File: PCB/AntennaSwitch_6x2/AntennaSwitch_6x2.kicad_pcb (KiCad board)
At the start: 2 copper layers, 100 x 100 mm, 160 parts, among them J1 Conn_01x08, J2 Conn_01x08, J3 Conn_01x08, J4 HR913550A, J5 SWD, J6 485, J7 12VDC, J8 Conn_01x01, Q1 2N7002K, SW1 LOAD, SW2 SRBV170501, SW3 SRBV170501, SW4 M/R, SW5 RESET, U1 74HC238, U10 74HC148, U11 74HC148, U12 4511, U13 4511, U14 Blue 0.59'', U15 Blue 0.59'', U16 STM32F030F4Px, U17 MAX485E, U18 CH395Q, U19 AZ1117-1.8, U2 74HC573, U20 SY8303, U3 74HC573, U4 74HC238, U5 74HC00, U6 74HC00, U7 74HC00, U8 74HC04, U9 TLC555, Y1 30MHz

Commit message: Relay Board SCH
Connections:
- net GND renamed chasis
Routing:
- net Net-(R68-Pad2): track 30.4 -> 20.7 mm
- net +3V3: track 887.9 -> 886.3 mm
- net /Remote/SWDIO: track 18.4 -> 16.9 mm
- net /Remote/SWCLK: track 20.7 -> 19.3 mm
- net chasis: track 201.3 -> 201.5 mm, vias 184 -> 185
- net +12V: vias 0 -> 3
- net (no net): vias 5 -> 1
- added copper zone on F.Cu, net GND
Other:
- net class CHASIS added: clearance 0.508, trace_width 0.2032, via_dia 0.8, via_drill 0.4

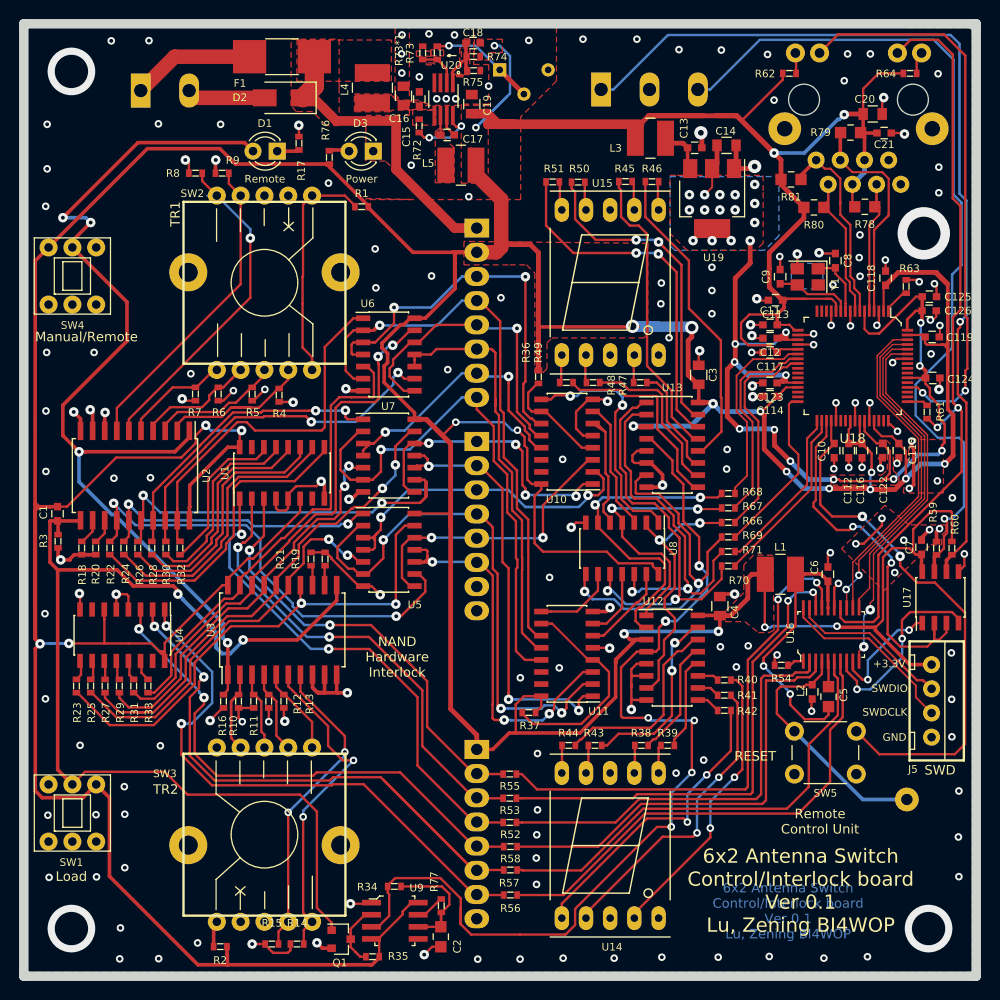
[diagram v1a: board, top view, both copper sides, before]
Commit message: Relay Board PCB first draft
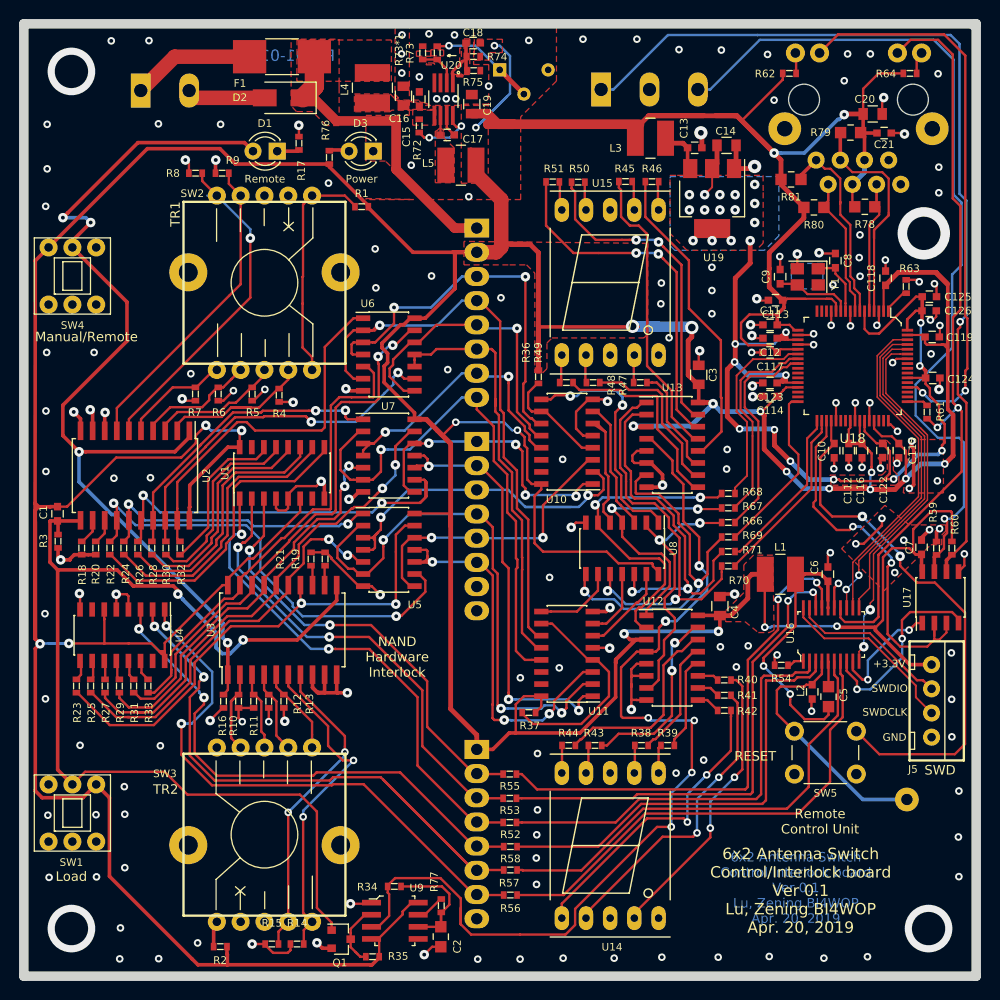
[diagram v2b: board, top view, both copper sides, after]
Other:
- board text added: "6x2 Antenna Switch Control/Interlock board Ver 0.1 Lu, Zening BI4WOP Apr. 20, 2019"
- board text added: "P0001-01"
- board text removed: "6x2 Antenna Switch Control/Interlock board Ver 0.1 Lu, Zening BI4WOP"

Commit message: manufacturing files
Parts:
- added REF**: M3_Screwhole, MyPCBLib:M3_Screwhole, F.Cu at (54.0, 54.0)
- U1, U10, U11, U12, U13, U4: footprint Housings_SOIC:SOIC-16_3.9x9.9mm_Pitch1.27mm -> digikey-footprints:SOIC-16_W3.90mm
- U17: footprint Housings_SOIC:SOIC-8_3.9x4.9mm_Pitch1.27mm -> digikey-footprints:SOIC-8_W3.9mm
- U2, U3: footprint Housings_SOIC:SOIC-20W_7.5x12.8mm_Pitch1.27mm -> MyPCBLib:SOIC-20_W7.5mm
- U5, U6, U7, U8: footprint Housings_SOIC:SOIC-14_3.9x8.7mm_Pitch1.27mm -> digikey-footprints:SOIC-14_W3.9mm
- moved U17 0.25 mm to (146.2, 110.0), turned to 0 degrees
- moved U3 0.09 mm to (77.1, 113.7), turned to 0 degrees
- turned U2 to 180 degrees
- turned U1 to 0 degrees
- turned U10 to 90 degrees
- turned U11 to 90 degrees
- turned U12 to 270 degrees
- turned U13 to 270 degrees
- turned U4 to 180 degrees
- turned U5 to 270 degrees
- turned U6 to 270 degrees
- turned U7 to 270 degrees
- turned U8 to 180 degrees
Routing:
- net +3V3: track 886.3 -> 971.1 mm
- net /Remote/RST: track 83.6 -> 88.8 mm
- net /Remote/TXD: track 20.5 -> 21.4 mm
- net chasis: vias 185 -> 183
- removed copper zone on F.Cu, net GND
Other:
- rule solder_mask_min_width: 0.25 -> 0.0762
- rule via_min_size: 0.4 -> 0.6

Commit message: FS Tools
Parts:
- added REF**: M3_Screwhole, MyPCBLib:M3_Screwhole, F.Cu at (144.4, 72.0)
- added REF**: M3_Screwhole, MyPCBLib:M3_Screwhole, F.Cu at (55.0, 145.0)
- added REF**: M3_Screwhole, MyPCBLib:M3_Screwhole, F.Cu at (145.0, 145.0)
- Q1: value 2N7002K -> 2N7002; footprint TO_SOT_Packages_SMD:SOT-23 -> lc_lib:SOT-23(SOT-23-3)
- R38, R39, R40, R41, R42, R43, R44, R45, R46, R47, R48, R49, R50, R51: value 81 -> 33
- U14, U15: value Blue 0.59'' -> Blue 0.56'' CC
- U16: footprint digikey-footprints:TSSOP-20_W4.4mm -> lc_lib:TSSOP-20
- moved Q1 0.27 mm to (83.1, 146.1), turned to 270 degrees
- renumbered REF** to e
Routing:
- net /Interlock/Load: track 112.4 -> 114.5 mm
- net chasis: track 201.5 -> 202.9 mm
- net Net-(Q1-Pad3): track 7.04 -> 8.35 mm
- net +12V: vias 3 -> 0
